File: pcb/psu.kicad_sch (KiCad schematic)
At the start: 14 parts, among them CN1 WJ15EDGK-3.81-02P-14-00A, P1 WJ15EDGRC-3.81-2P, U11 15uH, U6 LMR38020SDDAR

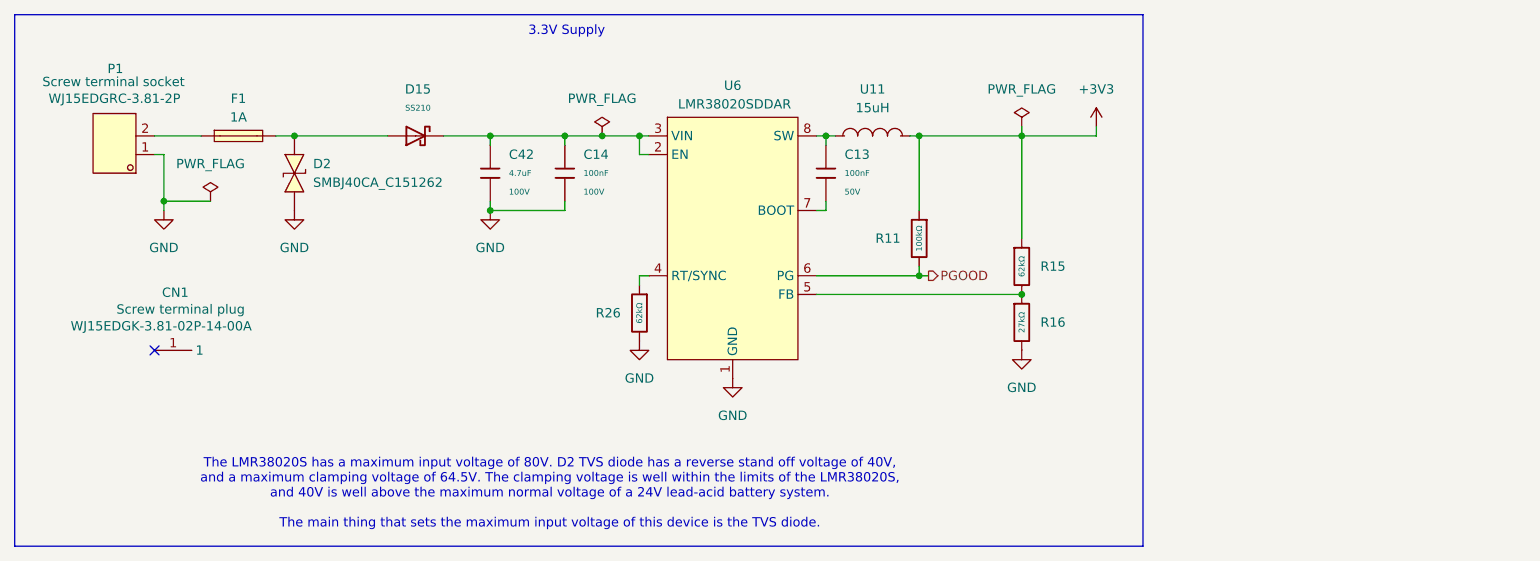
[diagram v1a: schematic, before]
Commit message: sch: add missing psu output capacitance
Forgot to add output capcitance to the 3.3V PSU
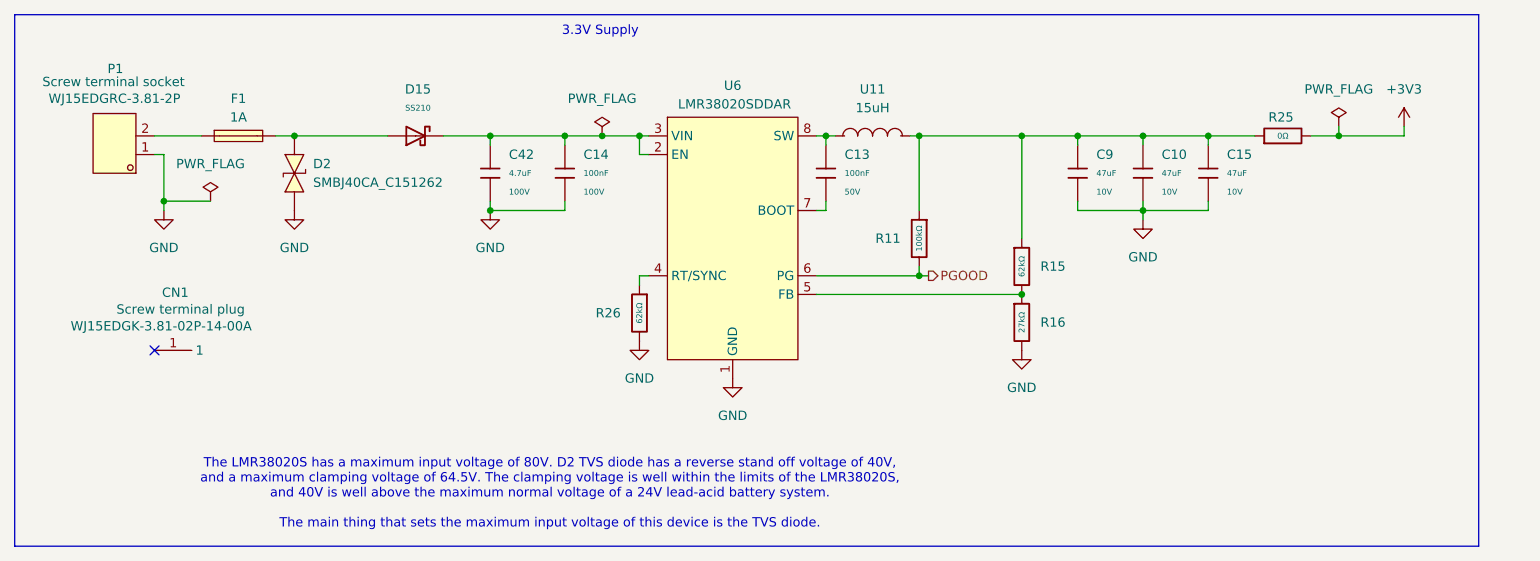
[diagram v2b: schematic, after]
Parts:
- added C10, C15, C9: 47uF, PCM_JLCPCB:C_1206, symbol PCM_JLCPCB-Capacitors:1206,47uF
- added R25: 0Ω, PCM_JLCPCB:R_0603, symbol PCM_JLCPCB-Resistors:0603,0Ω
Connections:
- net +3V3: now also R25.2; no longer R11.1, R15.1, U11.2
- net GND: now also C10.2, C15.2, C9.2
- new net: C10.1, C15.1, C9.1, R11.1, R15.1, R25.1, U11.2

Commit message: sch: add more input capacitance for 3.3v psu
Input capacitance was quite low, especially considering MLCC derating
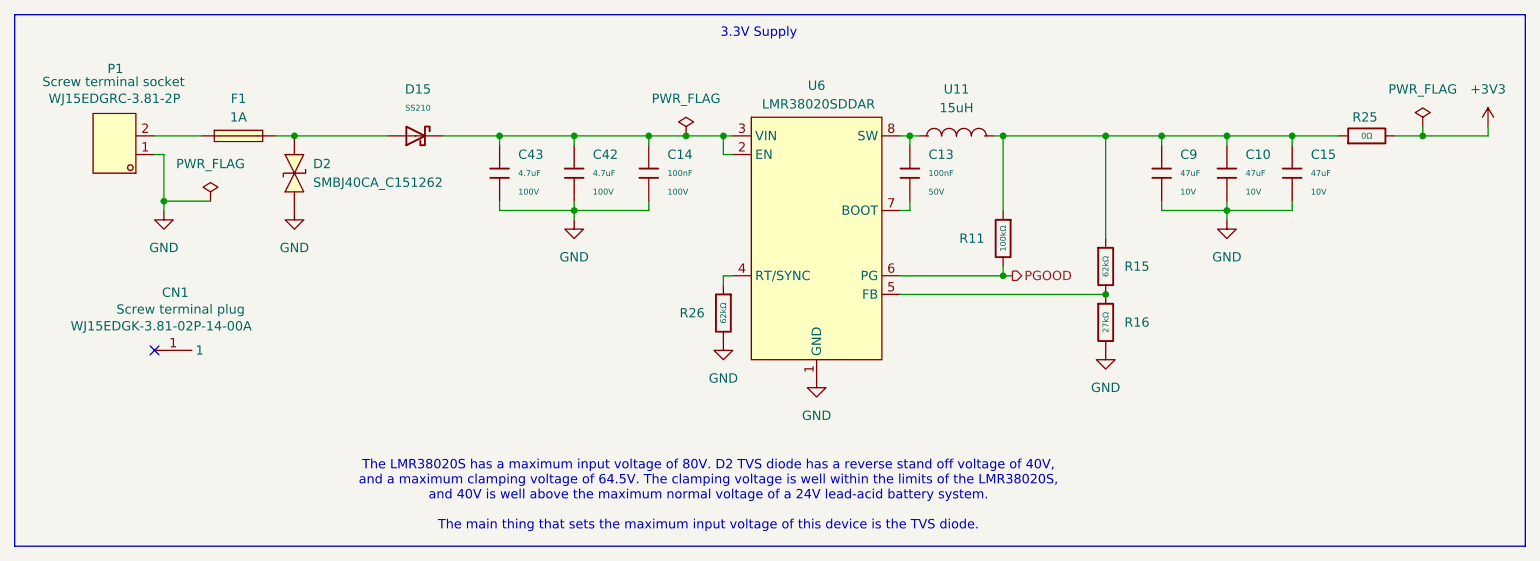
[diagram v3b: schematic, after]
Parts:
- added C43: 4.7uF, PCM_JLCPCB:C_1206, symbol PCM_JLCPCB-Capacitors:0805,100nF
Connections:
- net GND: now also C43.2
- net at C14.1, C42.1, D15.1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: now also C43.1
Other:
- moved on the sheet: C10, C13, C14, C15, C42, C9, R11, R15, R16, R25, R26, U11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

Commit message: sch: add test point for protected battery vin rail
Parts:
- added TP36: VIN_PROTECTED, TestPoint:TestPoint_Plated_Hole_D2.0mm, symbol Connector:TestPoint_Square
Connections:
- net at C14.1, C42.1, C43.1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: now also TP36.1
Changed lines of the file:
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@@
 	(wire
 		(pts
-			(xy 81.28 31.75) (xy 91.44 31.75)
+			(xy 91.44 31.75) (xy 81.28 31.75)
 		)
 		(stroke
@@
 	(wire
 		(pts
+			(xy 91.44 27.94) (xy 91.44 31.75)
+		)
+		(stroke
+			(width 0)
+			(type default)
+		)
+	)
+	(wire
+		(pts
 			(xy 34.29 31.75) (xy 40.64 31.75)
 		)
@@
 					(unit 1)
 				)
+			)
+		)
+	)
+	(symbol
+		(lib_id "Connector:TestPoint_Square")
+		(at 91.44 27.94 90)
+		(unit 1)
+		(body_style 1)
+		(exclude_from_sim no)
+		(in_bom no)
+		(on_board yes)
+		(in_pos_files no)
+		(dnp no)
+		(fields_autoplaced yes)
+		(property "Reference" "TP36"
+			(at 91.44 22.86 90)
+			(show_name no)
+			(do_not_autoplace no)
+			(effects
+				(font
+					(size 1.27 1.27)
+				)
+			)
+		)
+		(property "Value" "VIN_PROTECTED"
+			(at 91.44 25.4 90)
+			(show_name no)
+			(do_not_autoplace no)
+			(effects
+				(font
+					(size 1.27 1.27)
+				)
+			)
+		)
+		(property "Footprint" "TestPoint:TestPoint_Plated_Hole_D2.0mm"
+			(at 91.44 22.86 0)
+			(hide yes)
+			(show_name no)
+			(do_not_autoplace no)
+			(effects
+				(font
+					(size 1.27 1.27)
+				)
+			)
+		)
+		(property "Datasheet" "~"
+			(at 91.44 22.86 0)
+			(hide yes)
+			(show_name no)
+			(do_not_autoplace no)
+			(effects
+				(font
+					(size 1.27 1.27)
+				)
+			)
+		)
+		(property "Description" "test point"
+			(at 91.44 27.94 0)
+			(hide yes)
+			(show_name no)
+			(do_not_autoplace no)
+			(effects
+				(font
+					(size 1.27 1.27)
+				)
+			)
+		)
+		(property "Average Rectified Current (Io)" ""
+			(at 91.44 27.94 0)
+			(hide yes)
+			(show_name no)
+			(do_not_autoplace no)
+			(effects
+				(font
+					(size 1.27 1.27)
+				)
+			)
+		)
+		(property "Clamping Voltage" ""
+			(at 91.44 27.94 0)
+			(hide yes)
+			(show_name no)
+			(do_not_autoplace no)
+			(effects
+				(font
+					(size 1.27 1.27)
+				)
+			)
+		)
+		(property "LSCS Part" ""
+			(at 91.44 27.94 0)
+			(hide yes)
+			(show_name no)
+			(do_not_autoplace no)
+			(effects
+				(font
+					(size 1.27 1.27)
+				)
+			)
+		)
+		(property "Number of Channels" ""
+			(at 91.44 27.94 0)
+			(hide yes)
+			(show_name no)
+			(do_not_autoplace no)
+			(effects
+				(font
+					(size 1.27 1.27)
+				)
+			)
+		)
+		(property "Peak Pulse Current (Ipp)" ""
+			(at 91.44 27.94 0)
+			(hide yes)
+			(show_name no)
+			(do_not_autoplace no)
+			(effects
+				(font
+					(size 1.27 1.27)
+				)
+			)
+		)
+		(property "Peak Pulse Power Dissipation (Ppp)" ""
+			(at 91.44 27.94 0)
+			(hide yes)
+			(show_name no)
+			(do_not_autoplace no)
+			(effects
+				(font
+					(size 1.27 1.27)
+				)
+			)
+		)
+		(property "Peak forward surge current" ""
+			(at 91.44 27.94 0)
+			(hide yes)
+			(show_name no)
+			(do_not_autoplace no)
+			(effects
+				(font
+					(size 1.27 1.27)
+				)
+			)
+		)
+		(property "Polarity" ""
+			(at 91.44 27.94 0)
+			(hide yes)
+			(show_name no)
+			(do_not_autoplace no)
+			(effects
+				(font
+					(size 1.27 1.27)
+				)
+			)
+		)
+		(property "Voltage - Breakdown" ""
+			(at 91.44 27.94 0)
+			(hide yes)
+			(show_name no)
+			(do_not_autoplace no)
+			(effects
+				(font
+					(size 1.27 1.27)
+				)
+			)
+		)
+		(property "level of protection" ""
+			(at 91.44 27.94 0)
+			(hide yes)
+			(show_name no)
+			(do_not_autoplace no)
+			(effects
+				(font
+					(size 1.27 1.27)
+				)
+			)
+		)
+		(pin "1"
+		)
+		(instances
+			(project "EveningStar"
+				(path "/4c61f5a2-f8d4-462a-9bc3-d74437d30372/2e538fbd-4766-4d3c-804f-b602af6e3385"
+					(reference "TP36")
+					(unit 1)
+				)

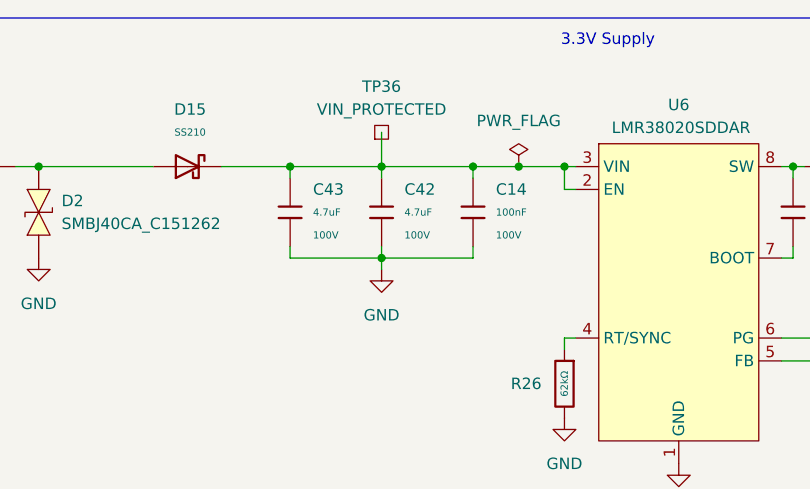
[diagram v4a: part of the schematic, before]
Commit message: sch: replace input caps with electrolytic
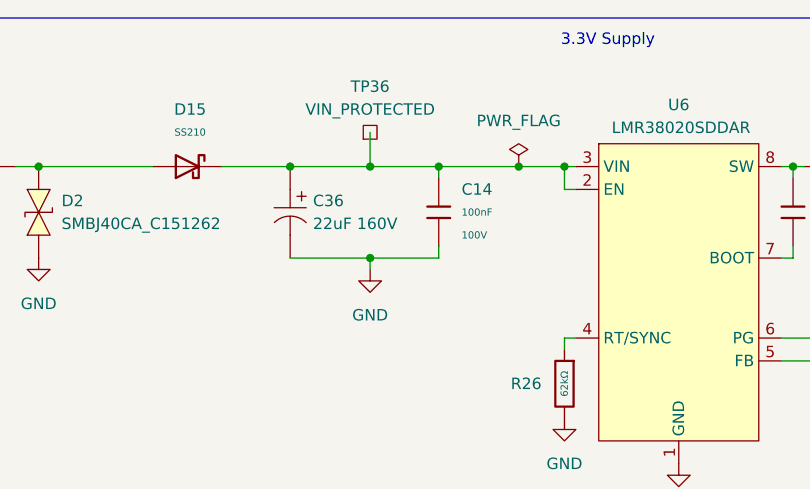
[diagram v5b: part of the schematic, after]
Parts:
- removed C42, C43: 4.7uF, PCM_JLCPCB:C_1206, symbol PCM_JLCPCB-Capacitors:0805,100nF
- added C36: 22uF 160V, EasyEDA:CAP-SMD_BD10.0-L10.3-W10.3-FD, symbol EasyEDA:ULV2C220MNL1GS
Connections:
- net GND: now also C36.2
- net at C14.1, D15.1, TP36.1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: now also C36.1
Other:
- moved on the sheet: C14, TP36

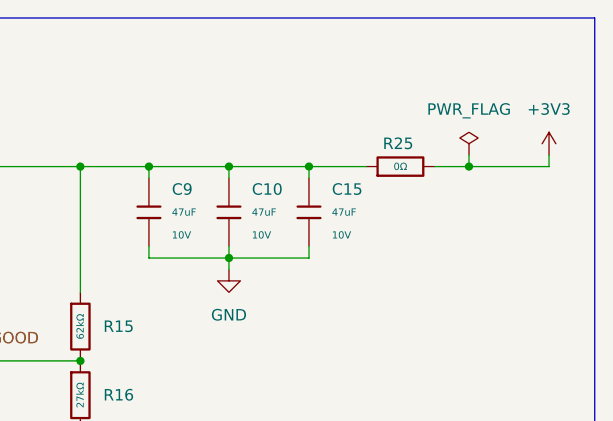
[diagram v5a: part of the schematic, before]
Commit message: pcb(psu): layout dc-dc converter
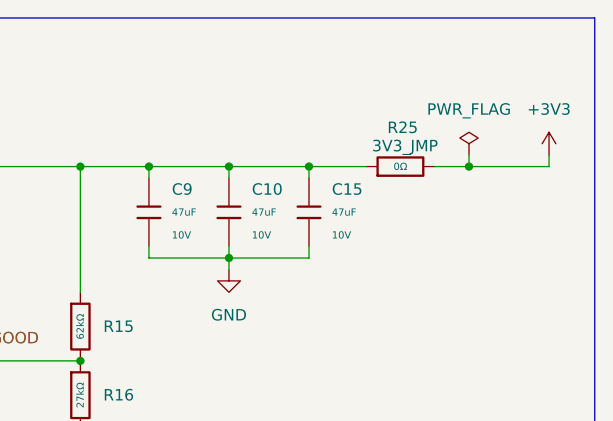
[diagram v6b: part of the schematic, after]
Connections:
- net GND: now also U6.9 (GND)
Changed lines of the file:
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@@
 		(pin "7"
+		)
+		(pin "9"
 		)
 		(instances
@@
 		(dnp no)
 		(property "Reference" "R25"
-			(at 199.136 29.21 90)
+			(at 199.644 27.432 90)
 			(show_name no)
 			(do_not_autoplace no)
@@
 			)
 		)
-		(property "Description" "-55°C~+155°C 0Ω 100mW 75V Thick Film Resistor ±1% 0603 Chip Resistor - Surface Mount ROHS"
-			(at 199.39 31.75 0)
-			(hide yes)
+		(property "Description" "3V3_JMP"
+			(at 199.898 29.464 90)
 			(show_name no)
 			(do_not_autoplace no)
@@
 				(font
 					(size 1.27 1.27)
+					(thickness 0.1588)
 				)
 			)

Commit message: pcb: fix most drc errors
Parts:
- TP36: footprint TestPoint:TestPoint_Plated_Hole_D2.0mm -> custom:TestPoint_Plated_Hole_D2.0mm
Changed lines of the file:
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@@
 			)
 		)
-		(property "Footprint" "TestPoint:TestPoint_Plated_Hole_D2.0mm"
+		(property "Footprint" "custom:TestPoint_Plated_Hole_D2.0mm"
 			(at 90.17 22.86 0)
 			(hide yes)

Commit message: pcb(silkscreen): fix power socket silkscreen clipping
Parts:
- P1: footprint EasyEDA:CONN-TH_2P-P3.81_WJ15EDGRC-3.81-2P -> custom:CONN-TH_2P-P3.81_WJ15EDGRC-3.81-2P_CLIPPED
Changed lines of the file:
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@@
 			)
 		)
-		(property "Footprint" "EasyEDA:CONN-TH_2P-P3.81_WJ15EDGRC-3.81-2P"
+		(property "Footprint" "custom:CONN-TH_2P-P3.81_WJ15EDGRC-3.81-2P_CLIPPED"
 			(at 30.48 24.13 0)
 			(hide yes)
